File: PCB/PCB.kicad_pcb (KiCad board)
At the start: 2 copper layers, 99 x 56.3 mm, 116 parts, among them J1 Termocouple_2, J10 2x5_2.54mm, J12 SSR2, J13 14x1-2.54mm, J14 USB_C_Receptacle_USB2.0, J2 PWR_IN, J3 Conn_01x02_Pin, J4 4x1-2.54mm, J5 Termocouple_1, J6 OUT2, J7 OUT1, J8 SSR1, Q1 BC817, Q2 BC817, Q3 BC817, Q4 BC817, Q5 AP30N03DF, SW1 SW_DPDT, SW2 SW_SPST, U1 MAX31855KASA, U2 MAX31855KASA, U4 MP2303ADN, U5 STM32F411CEUx, U6 CH340G, U7 W25Q16JVSNIQ, Y1 12MHz, Y3 12MHz

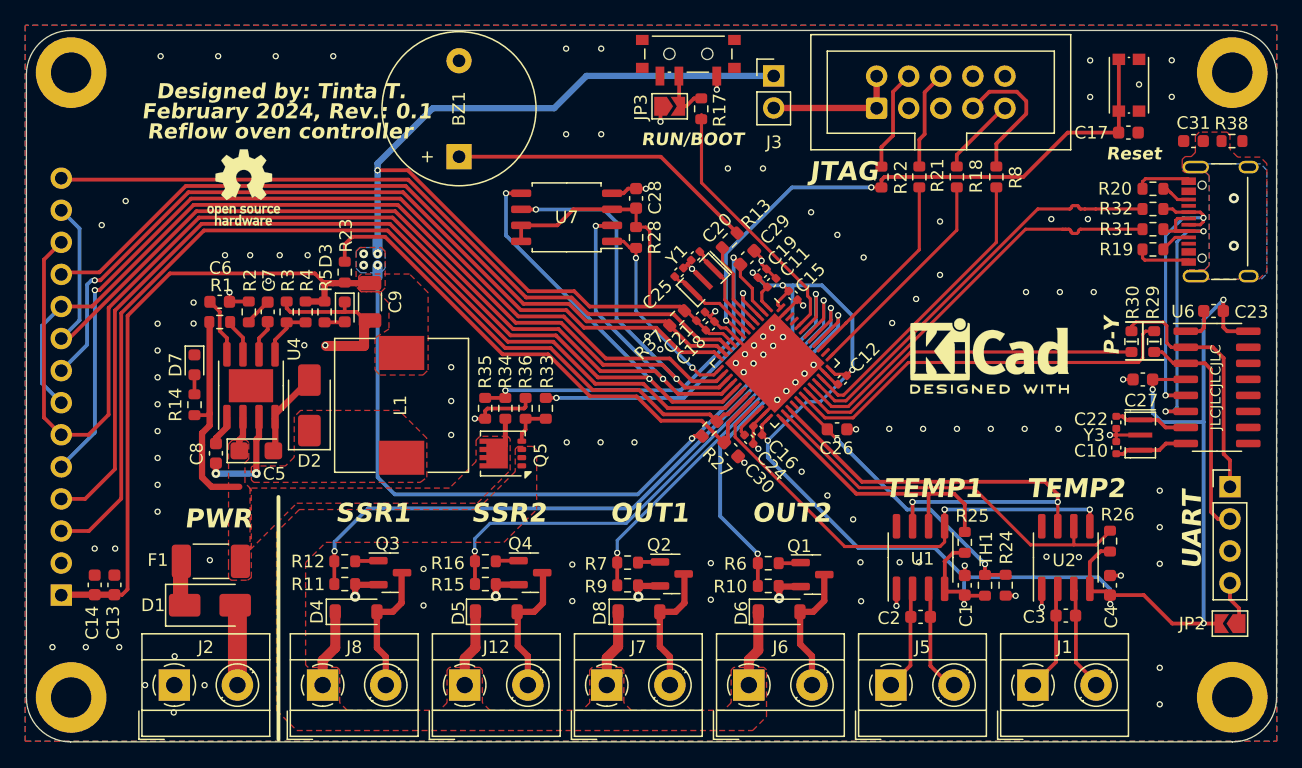
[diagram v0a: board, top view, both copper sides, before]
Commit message: PCB done and ordered, touch screen and TFT works, flash works, EdternalLoader, GUI partialy done
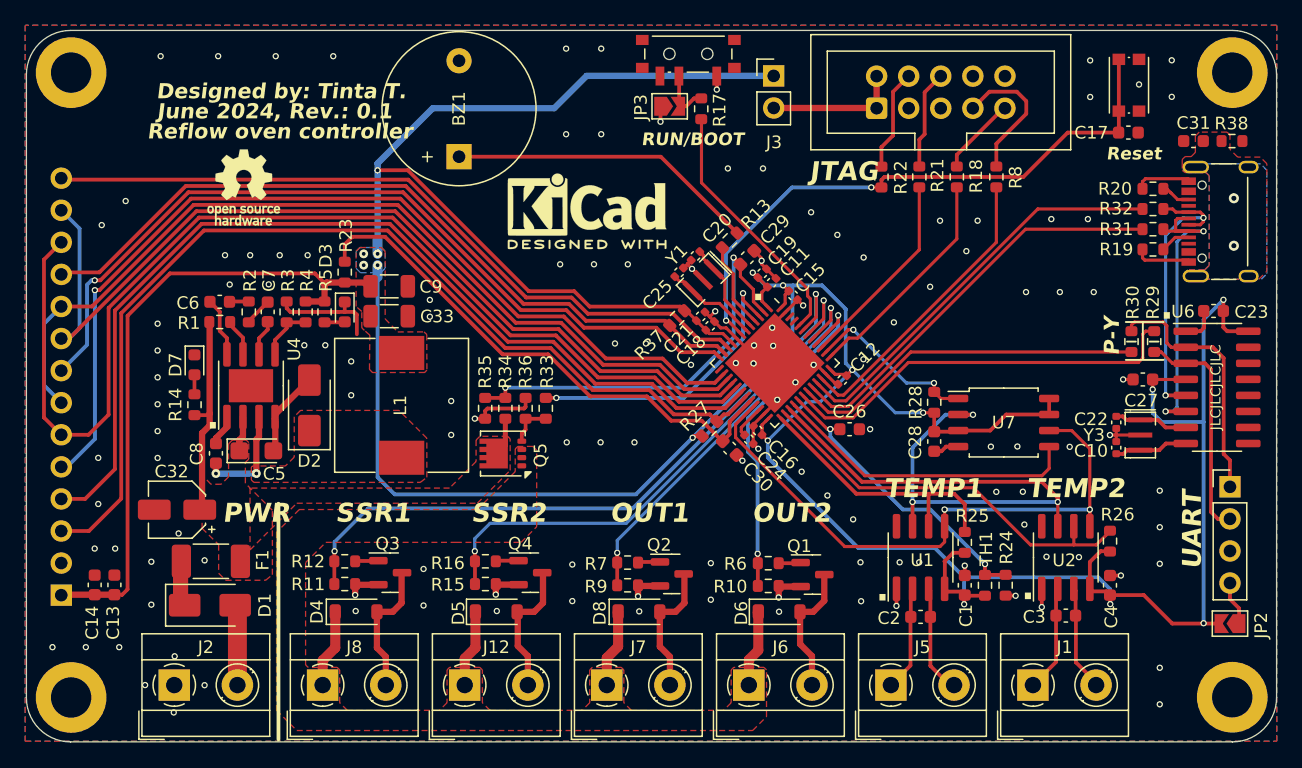
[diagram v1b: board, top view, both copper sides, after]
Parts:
- added C32: 4.7uF, Capacitor_SMD:CP_Elec_4x5.4, F.Cu at (121.7, 97.6)
- added C33: 22uF, Capacitor_SMD:C_1206_3216Metric, F.Cu at (138.5, 82.3)
- moved U7 38.2 mm to (187.2, 90.7), turned to 0 degrees
- moved REF** 33.9 mm to (154.2, 74.0)
- moved C28 30.5 mm to (181.7, 92.2), turned to 90 degrees
- moved R28 27.0 mm to (181.7, 89.1), turned to 90 degrees
- moved C9 1.95 mm to (138.5, 79.9), turned to 180 degrees
- moved C26 0.99 mm to (175.0, 91.2)
- moved C30 0.16 mm to (165.5, 92.7)
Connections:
- U5 pad 13: /CS_FLASH -> unconnected-(U5-PA3-Pad13)
- U5 pad 28: unconnected-(U5-PB15-Pad28) -> /MOSI_TC
- U5 pad 38: unconnected-(U5-PA15-Pad38) -> /CS_FLASH
- U7 pad 2: /MISO_TFT -> /MISO_TC
- U7 pad 5: /MOSI_TFT -> /MOSI_TC
- U7 pad 6: /SCK_TFT -> /SCK_TC
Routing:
- net /MOSI_TC: track 0.00 -> 24.5 mm
- net /SCK_TFT: track 93.7 -> 71.3 mm, vias 2 -> 0
- net /MOSI_TFT: track 109.1 -> 88.5 mm, vias 2 -> 0
- net /MISO_TFT: track 90.7 -> 75.6 mm, vias 2 -> 0
- net /MISO_TC: track 40.0 -> 51.1 mm, vias 2 -> 3
- net /SCK_TC: track 38.9 -> 47.5 mm
- net GND: track 94.9 -> 87.0 mm, vias 127 -> 133
- net /CS_FLASH: track 16.0 -> 13.9 mm
- net /OUT2: track 29.5 -> 27.7 mm
- net /AN_T1: track 22.7 -> 23.9 mm
- net +12V: track 23.1 -> 22.5 mm
- net +3.3V: track 342.6 -> 342.2 mm, vias 16 -> 17
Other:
- board text added: "."
- board text added: "June 2024, Rev.: 0.1"
- board text removed: "February 2024, Rev.: 0.1"

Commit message: PCB works (Problems: safety switch, analog inputs mistake), ExternalLoader works, gui in progress
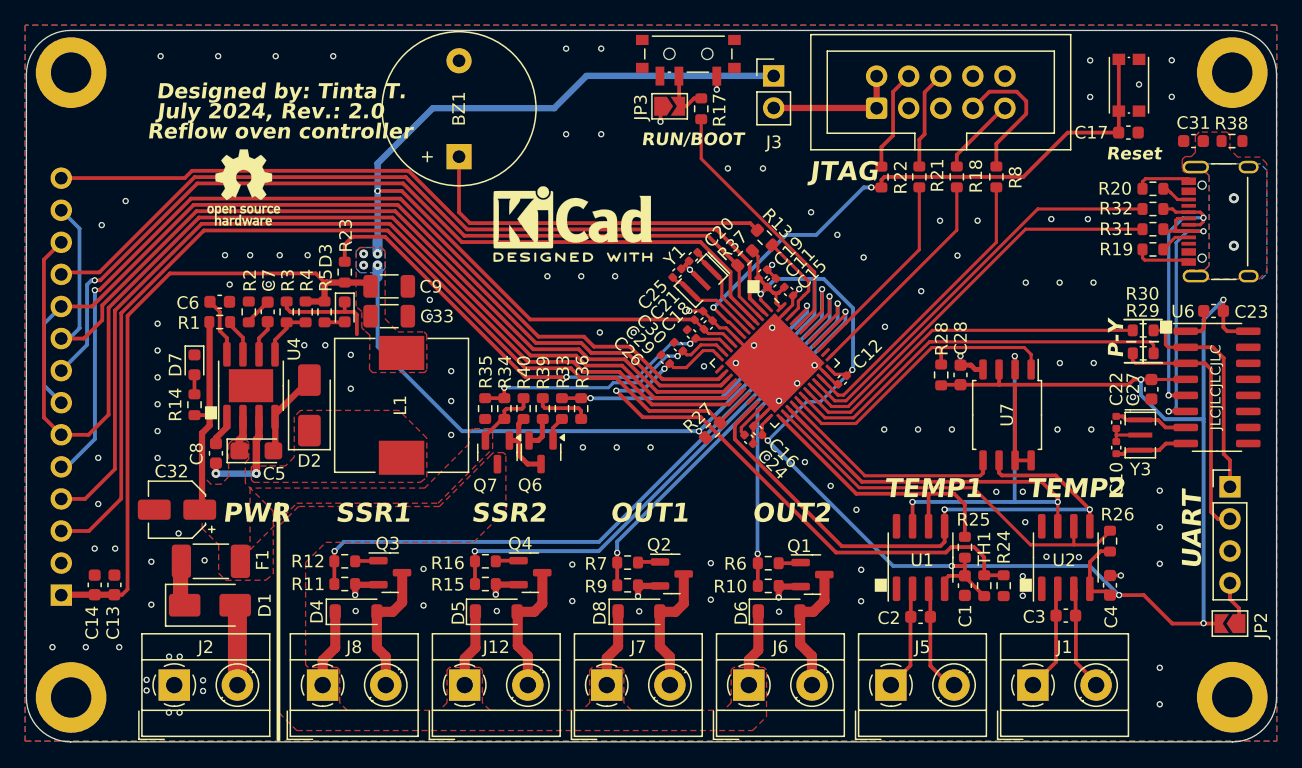
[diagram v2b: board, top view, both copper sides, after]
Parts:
- removed Q5: AP30N03DF, Package_SON:Diodes_PowerDI3333-8
- added Q6: BC817, Package_TO_SOT_SMD:SOT-23, F.Cu at (150.5, 93.1)
- added Q7: AO3401A, Package_TO_SOT_SMD:SOT-23, F.Cu at (147.1, 93.1)
- added R39: 1k, Resistor_SMD:R_0603_1608Metric, F.Cu at (150.7, 89.6)
- added R40: 10k, Resistor_SMD:R_0603_1608Metric, F.Cu at (149.2, 89.6)
- C26, C29, C30: footprint Capacitor_SMD:C_0603_1608Metric -> Capacitor_SMD:C_0402_1005Metric
- C33, C9: value 22uF -> 4.7uF
- R34: value 6k8 -> 10k
- R35: value 1k -> 1k8
- moved C26 15.6 mm to (160.4, 85.7), turned to -45 degrees
- moved C30 9.53 mm to (162.5, 83.7), turned to -45 degrees
- moved C29 8.90 mm to (161.4, 84.7), turned to -45 degrees
- moved R37 7.18 mm to (166.7, 77.7)
- moved C28 5.67 mm to (183.8, 86.9), turned to -90 degrees
- moved R36 4.40 mm to (153.7, 89.6), turned to 90 degrees
- moved R13 2.78 mm to (168.3, 76.1), turned to -45 degrees
- moved R28 2.24 mm to (182.2, 86.9)
- moved REF** 1.52 mm to (153.1, 75.0)
- moved R30 1.28 mm to (198.2, 83.4), turned to 0 degrees
- moved R33 1.28 mm to (152.2, 89.6)
- moved R29 1.27 mm to (198.2, 85.2), turned to 180 degrees
- moved C27 1.03 mm to (198.9, 88.1), turned to 90 degrees
- moved U7 0.66 mm to (187.4, 90.1), turned to -90 degrees
- moved C15 0.47 mm to (170.2, 80.3)
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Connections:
- R33 pad 2: Net-(Q5-G) -> Net-(Q6-B)
- R36 pad 2: Net-(Q5-G) -> /INHIBIT
- U5 pad 10: /IRQ_TP -> /AN_3V3
- U5 pad 11: /CS_TP -> /AN_12V
- U5 pad 12: /LED_TFT -> /AN_T1
- U5 pad 2: /AN_12V -> /IRQ_TP
- U5 pad 20: /AN_3V3 -> unconnected-(U5-PB2-Pad20)
- U5 pad 29: /AN_T1 -> /CS_FLASH
- U5 pad 3: /INHIBIT -> /CS_TP
- U5 pad 38: /CS_FLASH -> unconnected-(U5-PA15-Pad38)
- U5 pad 4: /BUZZER -> /LED_TFT
- U5 pad 45: unconnected-(U5-PB8-Pad45) -> /INHIBIT
- U5 pad 46: unconnected-(U5-PB9-Pad46) -> /BUZZER
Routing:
- net /AN_T1: track 23.9 -> 47.9 mm
- net /AN_12V: track 33.8 -> 21.7 mm
- net /CS_FLASH: track 13.9 -> 24.4 mm, vias 2 -> 0
- net GND: track 87.0 -> 77.8 mm, vias 133 -> 132
- net /MOSI_TC: track 24.5 -> 18.4 mm
- net +3.3V: track 342.2 -> 336.3 mm, vias 17 -> 15
- net Net-(Q6-C): track 0.00 -> 5.82 mm
- net /AN_3V3: track 42.6 -> 38.0 mm, vias 0 -> 2
- net Net-(BZ1--): track 24.5 -> 28.6 mm
- net /IRQ_TP: track 58.4 -> 62.3 mm
- net Net-(Q5-G): track 3.50 -> 0.00 mm
- net /LED_TFT: track 66.2 -> 69.5 mm
- net /CS_TP: track 61.1 -> 64.4 mm
- net Net-(Q6-E): track 0.00 -> 2.65 mm
- net +12V: track 22.5 -> 25.0 mm
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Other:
- board text added: "July 2024, Rev.: 2.0"
- board text removed: "June 2024, Rev.: 0.1"

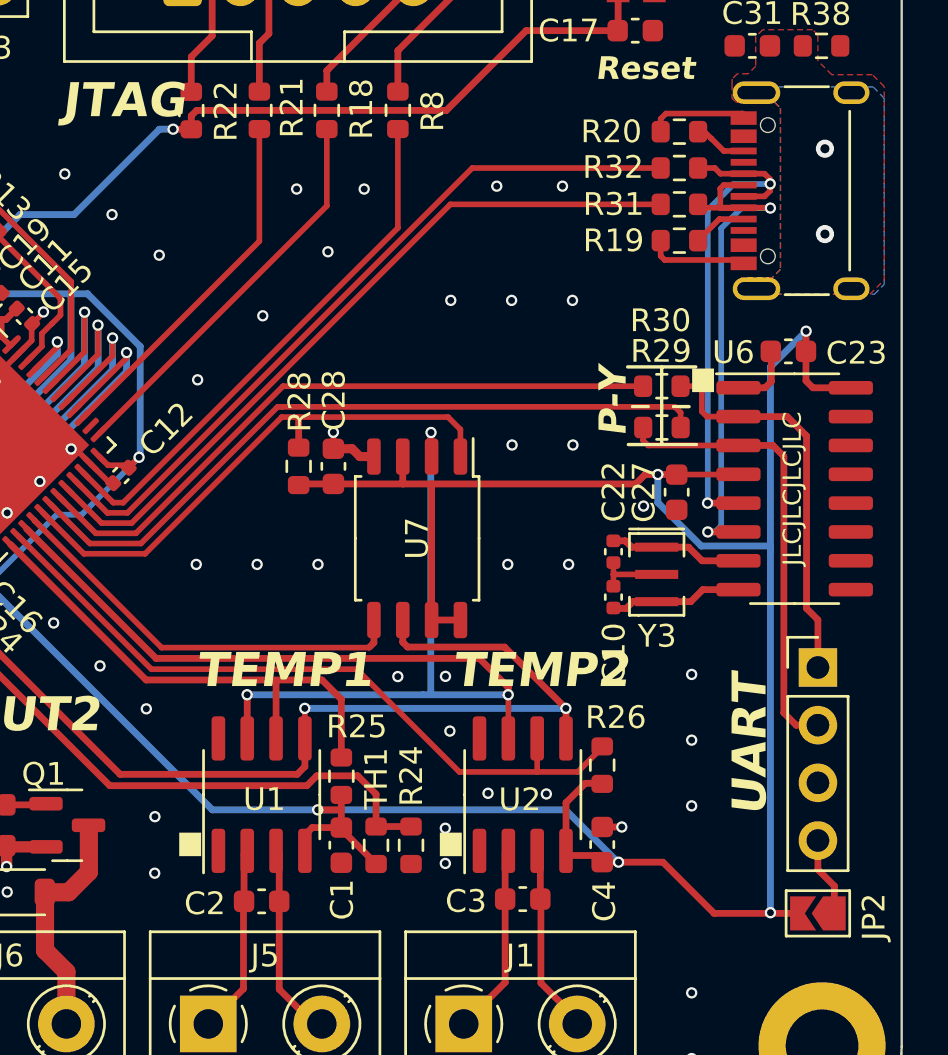
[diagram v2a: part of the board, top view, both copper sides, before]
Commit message: PCB update, firmaware
usb problem -> repaired

firmware update: pid, PWM, gui
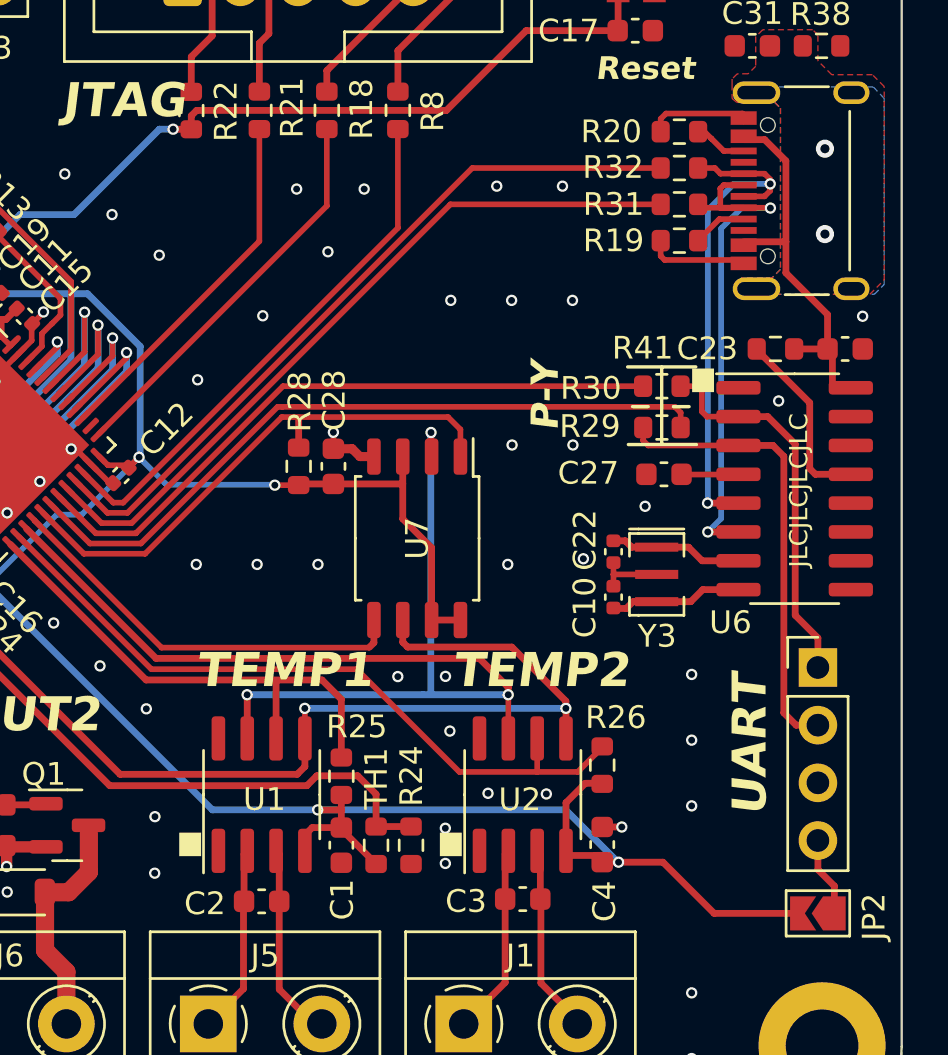
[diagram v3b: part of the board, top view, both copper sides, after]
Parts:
- added R41: 10k, Resistor_SMD:R_0603_1608Metric, F.Cu at (203.2, 81.8)
- moved C23 2.50 mm to (206.3, 81.8), turned to 180 degrees
- moved C27 0.97 mm to (198.3, 87.3), turned to 0 degrees
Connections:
- C23 pad 2: +3.3V -> +5V
- C27 pad 2: +3.3V -> Net-(U6-V3)
- J14 pad A4: unconnected-(J14-VBUS-PadA4) -> +5V
- J14 pad A9: unconnected-(J14-VBUS-PadA4)_2 -> +5V
- J14 pad B4: unconnected-(J14-VBUS-PadA4)_1 -> +5V
- J14 pad B9: unconnected-(J14-VBUS-PadA4)_0 -> +5V
- U6 pad 13: unconnected-(U6-~{DTR}-Pad13) -> Net-(U6-~{DTR})
- U6 pad 16: +3.3V -> +5V
- U6 pad 4: +3.3V -> Net-(U6-V3)
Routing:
- net +3.3V: track 336.3 -> 291.9 mm, vias 15 -> 13
- net +5V: track 0.00 -> 17.2 mm
- net Net-(U6-~{DTR}): track 0.00 -> 8.15 mm
- net GND: track 77.8 -> 74.9 mm, vias 132 -> 134
- net Net-(U6-V3): track 0.00 -> 2.54 mm
- net /TXD: track 46.5 -> 46.0 mm
